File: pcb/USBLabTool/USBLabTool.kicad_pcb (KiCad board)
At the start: 4 copper layers, 79.4 x 56.2 mm, 227 parts, among them J1 Conn_01x06_Pin, J17 2x01, J19 T_N5V, J2 Conn_02x12_Odd_Even, J20 USB_C_Receptacle, K1 G5V-2, K2 G5V-2, Q1 STL11N3LLH6, SW1 TS02-66-73-BK-100-SCR-D, U1 AQY284SX, U10 MC33274ADR2G, U11 DG403, U12 STM32H562VGTx, U13 R1283K002A, U14 ST1L05APU33R, U15 ST1L05APU33R, U16 LTC1983ES6-5TRMPBF, U17 TCPP01-M12, U18 74HC245, U19 USBLC6-2SC6, U2 AQY284SX, U20 74HC245, U3 CD74HC4316, U4 LMP7718, U5 CD74HC4316, U6 LMP7718, U7 OPA863, U8 OPA863, U9 MC33274ADR2G, Y1 32.768kHz, Y2 NX2016SA-25M-EXS00A-CS08742

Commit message: fixes
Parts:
- added JP3: SJ, Jumper:SolderJumper-2_P1.3mm_Open_RoundedPad1.0x1.5mm, F.Cu at (124.1, 67.7)
- added JP4: SJ, Jumper:SolderJumper-2_P1.3mm_Open_RoundedPad1.0x1.5mm, B.Cu at (138.8, 68.1)
- added JP5: SJ, Jumper:SolderJumper-2_P1.3mm_Open_RoundedPad1.0x1.5mm, B.Cu at (113.4, 72.2)
- added JP6: SJ, Jumper:SolderJumper-2_P1.3mm_Open_RoundedPad1.0x1.5mm, F.Cu at (150.9, 99.9)
- added JP7: SJ, Jumper:SolderJumper-2_P1.3mm_Open_RoundedPad1.0x1.5mm, F.Cu at (150.9, 102.8)
- added R82: 0, Resistor_SMD:R_0603_1608Metric_Pad0.98x0.95mm_HandSolder, B.Cu at (159.3, 94.4)
- added R83: 0, Resistor_SMD:R_0603_1608Metric_Pad0.98x0.95mm_HandSolder, B.Cu at (149.8, 94.1)
- added R84: 5.1k, Resistor_SMD:R_0603_1608Metric_Pad0.98x0.95mm_HandSolder, F.Cu at (140.7, 67.3)
- added R85: 5.1k, Resistor_SMD:R_0603_1608Metric_Pad0.98x0.95mm_HandSolder, B.Cu at (116.1, 76.8)
- C59, C60: value 4.7uF -> 100nF
- C70: value 10nF -> DNF
- L5, L6: value 47uH -> 4.7uH; footprint Inductor_SMD:L_0603_1608Metric_Pad1.05x0.95mm_HandSolder -> userfp:IND_TAIYO_NRH2410_TAY
- moved D1 1.19 mm to (186.7, 103.5)
- moved L6 0.91 mm to (187.1, 107.0)
- moved L5 0.88 mm to (136.9, 78.7)
- moved C75 0.58 mm to (147.3, 92.1)
- moved C72 0.31 mm to (131.9, 70.3)
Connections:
- C33 pad 1: RCC_OSC_IN -> Net-(JP6-B)
- C34 pad 2: RCC_OSC_OUT -> Net-(JP7-A)
- C35 pad 2: RCC_OSC32_IN -> Net-(C35-Pad2)
- C36 pad 2: RCC_OSC32_OUT -> Net-(C36-Pad2)
- C70 pad 1: +5V -> Net-(D10-A)
- C72 pad 2: UCPD_CC1 -> Net-(J20-CC1)
- C73 pad 2: UCPD_CC2 -> Net-(J20-CC2)
- C74 pad 2: +5V -> Net-(D10-A)
- D10 pad 2: +5V -> Net-(D10-A)
- D3 pad 1: +3.3VA -> GNDA
- D3 pad 2: GNDA -> +3.3VA
- D4 pad 1: +3.3VA -> GNDA
- D4 pad 2: GNDA -> +3.3VA
- D9 pad C: +5V -> Net-(D10-A)
- J20 pad A4: +5V -> Net-(D10-A)
- J20 pad A5: UCPD_CC1 -> Net-(J20-CC1)
- J20 pad A9: +5V -> Net-(D10-A)
- J20 pad B4: +5V -> Net-(D10-A)
- J20 pad B5: UCPD_CC2 -> Net-(J20-CC2)
- J20 pad B9: +5V -> Net-(D10-A)
- Q1 pad 5: +5V -> Net-(D10-A)
- R67 pad 1: +5V -> Net-(D10-A)
- U12 pad 52: UCPD_CC1 -> Net-(U12-PB13)
- U12 pad 53: UCPD_CC2 -> Net-(U12-PB14)
- U17 pad 7: UCPD_CC1 -> Net-(J20-CC1)
- U17 pad 9: UCPD_CC2 -> Net-(J20-CC2)
- Y1 pad 1: RCC_OSC32_OUT -> Net-(C36-Pad2)
- Y1 pad 2: RCC_OSC32_IN -> Net-(C35-Pad2)
- Y2 pad 1: RCC_OSC_IN -> Net-(JP6-B)
- Y2 pad 3: RCC_OSC_OUT -> Net-(JP7-A)
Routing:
- net Net-(D10-A): track 0.00 -> 84.6 mm, vias 0 -> 7
- net +5V: track 252.2 -> 211.6 mm, vias 11 -> 9
- net Net-(J20-CC1): track 0.00 -> 29.2 mm, vias 0 -> 3
- net Net-(J20-CC2): track 0.00 -> 27.9 mm, vias 0 -> 2
- net Net-(U12-PB13): track 0.00 -> 26.9 mm, vias 0 -> 3
- net Net-(U12-PB14): track 0.00 -> 26.4 mm, vias 0 -> 2
- net Net-(JP7-A): track 0.00 -> 18.4 mm, vias 0 -> 2
- net UCPD_CC1: track 37.8 -> 20.8 mm, vias 4 -> 1
- net RCC_OSC_OUT: track 8.50 -> 24.6 mm, vias 0 -> 2
- net Net-(JP6-B): track 0.00 -> 10.9 mm
- net UCPD_CC2: track 55.7 -> 48.7 mm, vias 5 -> 4
- net RCC_OSC_IN: track 4.02 -> 10.7 mm
- net Net-(C36-Pad2): track 0.00 -> 5.34 mm
- net Net-(C35-Pad2): track 0.00 -> 4.14 mm
- net +3.3V: track 141.5 -> 144.9 mm, vias 11 -> 13
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
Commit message: Update USBLabTool.kicad_pcb
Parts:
- moved JP7 1.20 mm to (151.8, 103.5)
- moved JP6 1.03 mm to (151.0, 101.0)
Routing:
- net RCC_OSC_IN: track 10.7 -> 11.7 mm
- net Net-(JP6-B): track 10.9 -> 11.9 mm
- net Net-(JP7-A): track 18.4 -> 17.7 mm
- net RCC_OSC_OUT: track 24.6 -> 24.0 mm
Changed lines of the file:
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@@
 		(tags "LQFP QFP")
 		(property "Reference" "U12"
-			(at -8.025 -7.95 0)
+			(at -7.794 -7.856 0)
 			(layer "F.SilkS")
 			(effects
@@
 	(footprint "Jumper:SolderJumper-2_P1.3mm_Open_RoundedPad1.0x1.5mm"
 		(layer "F.Cu")
-		(at 150.9 102.8 180)
+		(at 151.85 103.525 180)
 		(descr "SMD Solder Jumper, 1x1.5mm, rounded Pads, 0.3mm gap, open")
 		(tags "solder jumper open")
 		(property "Reference" "JP7"
-			(at 0 -1.8 0)
+			(at -3.1 0.025 0)
 			(layer "F.SilkS")
 			(effects
@@
 	(footprint "Jumper:SolderJumper-2_P1.3mm_Open_RoundedPad1.0x1.5mm"
 		(layer "F.Cu")
-		(at 150.95 99.925)
+		(at 151 100.95)
 		(descr "SMD Solder Jumper, 1x1.5mm, rounded Pads, 0.3mm gap, open")
 		(tags "solder jumper open")
 		(property "Reference" "JP6"
-			(at 0 -1.8 0)
+			(at -2.125 2 0)
 			(layer "F.SilkS")
 			(effects
@@
 	)
 	(gr_text "RESET"
-		(at 155.106 105.244 0)
+		(at 155.775 103.675 0)
 		(layer "F.SilkS")
 		(effects
@@
 	)
 	(segment
-		(start 150.3 99.1)
-		(end 150.3 99.925)
+		(start 152.625 92.625)
+		(end 152.625 97.85)
 		(width 0.2)
 		(layer "F.Cu")
@@
 	)
 	(segment
-		(start 152.625 96.775)
-		(end 150.3 99.1)
+		(start 150.35 100.125)
+		(end 150.35 100.95)
 		(width 0.2)
 		(layer "F.Cu")
@@
 	)
 	(segment
-		(start 152.625 92.625)
-		(end 152.625 96.775)
+		(start 152.625 97.85)
+		(end 150.35 100.125)
 		(width 0.2)
 		(layer "F.Cu")
@@
 	)
 	(segment
-		(start 156.5 97.45)
-		(end 156.5 100.075)
+		(start 149.331 91.294)
+		(end 148.375 92.25)
 		(width 0.2)
 		(layer "F.Cu")
@@
 	)
 	(segment
-		(start 149.331 91.294)
-		(end 148.375 92.25)
+		(start 156.5 97.45)
+		(end 156.525 97.425)
 		(width 0.2)
 		(layer "F.Cu")
@@
 	)
 	(segment
-		(start 151 101.5)
-		(end 150.25 102.25)
+		(start 151.2 103.525)
+		(end 151.2 102.95)
 		(width 0.2)
 		(layer "F.Cu")
@@
 	)
 	(segment
-		(start 156.525 97.425)
-		(end 156.5 97.45)
+		(start 151.875 102.275)
+		(end 154.3 102.275)
 		(width 0.2)
 		(layer "F.Cu")
@@
 	)
 	(segment
-		(start 150.25 102.25)
-		(end 150.25 102.8)
+		(start 151.2 102.95)
+		(end 151.875 102.275)
 		(width 0.2)
 		(layer "F.Cu")
@@
 	(segment
 		(start 156.5 100.075)
-		(end 155.075 101.5)
+		(end 156.5 97.45)
 		(width 0.2)
 		(layer "F.Cu")
@@
 	)
 	(segment
-		(start 155.375 96.275)
-		(end 156.525 97.425)
+		(start 154.3 102.275)
+		(end 156.5 100.075)
 		(width 0.2)
 		(layer "F.Cu")
@@
 	)
 	(segment
-		(start 155.075 101.5)
-		(end 151 101.5)
+		(start 156.525 97.425)
+		(end 155.375 96.275)
 		(width 0.2)
 		(layer "F.Cu")
@@
 	)
 	(segment
+		(start 129.215 70.79)
+		(end 129.215 72.915)
+		(width 0.2)
+		(layer "F.Cu")
+		(net 189)
+	)
+	(segment
 		(start 129.325 73.025)
 		(end 129.275 73.025)
@@
 	)
 	(segment
-		(start 129.275 73.025)
-		(end 126.556 75.744)
+		(start 129.215 72.915)
+		(end 129.325 73.025)
 		(width 0.2)
 		(layer "F.Cu")
@@
 	)
 	(segment
-		(start 129.215 70.79)
-		(end 129.215 72.735)
+		(start 129.275 73.025)
+		(end 126.556 75.744)
 		(width 0.2)
 		(layer "F.Cu")
@@
 	)
 	(segment
-		(start 153.435 91.91)
-		(end 153.435 93.25)
+		(start 151.925 99.6)
+		(end 154.775 96.75)
 		(width 0.2)
 		(layer "F.Cu")
@@
 	)
 	(segment
-		(start 151.6 99.925)
-		(end 154.775 96.75)
+		(start 153.435 91.91)
+		(end 153.435 93.25)
 		(width 0.2)
 		(layer "F.Cu")
@@
 	)
 	(segment
+		(start 151.65 100.95)
+		(end 151.65 99.875)
+		(width 0.2)
+		(layer "F.Cu")
+		(net 213)
+	)
+	(segment
 		(start 153.075 91.55)
 		(end 153.435 91.91)
@@
 	)
 	(segment
+		(start 151.65 99.875)
+		(end 151.925 99.6)
+		(width 0.2)
+		(layer "F.Cu")
+		(net 213)
+	)
+	(segment
 		(start 152.75 91.55)
 		(end 153.075 91.55)
@@
 	)
 	(segment
-		(start 153.375 102.8)
-		(end 151.55 102.8)
+		(start 154.35 102.75)
+		(end 153.425 102.75)
 		(width 0.2)
 		(layer "F.Cu")
@@
 	)
 	(segment
-		(start 156.975 100.125)
-		(end 154.35 102.75)
+		(start 152.65 103.525)
+		(end 152.5 103.525)
 		(width 0.2)
 		(layer "F.Cu")
@@
 	)
 	(segment
-		(start 154.35 102.75)
-		(end 153.425 102.75)
+		(start 154.975 90.5)
+		(end 155.25 90.775)
 		(width 0.2)
 		(layer "F.Cu")
@@
 	)
 	(segment
-		(start 156.95 96.85)
-		(end 156.975 96.875)
+		(start 156.975 100.125)
+		(end 154.35 102.75)
 		(width 0.2)
 		(layer "F.Cu")
@@
 	)
 	(segment
-		(start 156.975 96.875)
-		(end 156.975 100.125)
+		(start 154.1 90.5)
+		(end 154.975 90.5)
 		(width 0.2)
 		(layer "F.Cu")
@@
 	)
 	(segment
-		(start 154.975 90.5)
-		(end 155.25 90.775)
+		(start 156.975 96.875)
+		(end 156.975 100.125)
 		(width 0.2)
 		(layer "F.Cu")
@@
 	)
 	(segment
-		(start 154.1 90.5)
-		(end 154.975 90.5)
+		(start 153.425 102.75)
+		(end 152.65 103.525)
 		(width 0.2)
 		(layer "F.Cu")
@@
 	)
 	(segment
-		(start 153.425 102.75)
-		(end 153.375 102.8)
+		(start 156.95 96.85)
+		(end 156.875 96.925)
 		(width 0.2)
 		(layer "F.Cu")
@@
 	)
 	(segment
-		(start 156.95 96.85)
-		(end 156.875 96.925)
+		(start 155.7 91.225)
+		(end 155.7 93.25)
 		(width 0.2)
 		(layer "F.Cu")
@@
 	)
 	(segment
-		(start 155.7 91.225)
-		(end 155.7 93.25)
+		(start 156.95 96.85)
+		(end 156.975 96.875)
 		(width 0.2)
 		(layer "F.Cu")

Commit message: V2 fixed
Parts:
- added JP8: SJ, Jumper:SolderJumper-2_P1.3mm_Open_RoundedPad1.0x1.5mm, F.Cu at (160.7, 102.8)
- added JP9: SJ, Jumper:SolderJumper-2_P1.3mm_Open_RoundedPad1.0x1.5mm, F.Cu at (157.2, 102.8)
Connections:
- R82 pad 1: RCC_OSC32_IN -> Net-(JP8-B)
- R83 pad 1: RCC_OSC32_OUT -> Net-(JP9-B)
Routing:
- net Net-(JP9-B): track 0.00 -> 13.8 mm, vias 0 -> 2
- net Net-(JP8-B): track 0.00 -> 9.17 mm, vias 0 -> 1
- net RCC_OSC32_OUT: track 4.81 -> 13.1 mm, vias 1 -> 2
- net RCC_OSC32_IN: track 11.0 -> 16.5 mm, vias 1 -> 2
- net Net-(U15-VO): track 9.24 -> 12.2 mm
- net RCC_OSC_OUT: track 24.0 -> 23.0 mm
- net Net-(JP7-A): track 17.7 -> 16.9 mm

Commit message: PCB V2 updates
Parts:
- removed CR2: ESDALC6V1-1U2, userfp:DIODE_ESDALC6V1-1U2_STM
- removed JP8, JP9: SJ, Jumper:SolderJumper-2_P1.3mm_Open_RoundedPad1.0x1.5mm
- added CR1: ESDALC6V1-1M2, Diode_SMD:D_SOD-882, B.Cu at (148.8, 91.3)
- added H3: MountingHole, MountingHole:MountingHole_2.2mm_M2, F.Cu at (113.0, 79.2)
- added H4: MountingHole, MountingHole:MountingHole_2.2mm_M2, F.Cu at (186.2, 118.8)
- added TP15: TestPoint, TestPoint:TestPoint_Pad_2.0x2.0mm, B.Cu at (147.2, 79.8)
- added TP16: TestPoint, TestPoint:TestPoint_Pad_2.0x2.0mm, B.Cu at (129.3, 98.5)
- added TP17: TestPoint, TestPoint:TestPoint_Pad_2.0x2.0mm, B.Cu at (114.8, 102.0)
- added TP18: TestPoint, TestPoint:TestPoint_Pad_2.0x2.0mm, F.Cu at (154.6, 67.8)
- added TP19: TestPoint, TestPoint:TestPoint_Pad_2.0x2.0mm, F.Cu at (137.2, 75.4)
- added TP20: TestPoint, TestPoint:TestPoint_Pad_2.0x2.0mm, B.Cu at (143.8, 70.0)
- added TP21: TestPoint, TestPoint:TestPoint_Pad_2.0x2.0mm, B.Cu at (143.3, 79.8)
- added TP22: TestPoint, TestPoint:TestPoint_Pad_2.0x2.0mm, B.Cu at (183.4, 73.7)
- added TP23: TestPoint, TestPoint:TestPoint_Pad_2.0x2.0mm, B.Cu at (169.6, 73.0)
- added TP24: TestPoint, TestPoint:TestPoint_Pad_2.0x2.0mm, B.Cu at (142.8, 99.9)
- added TP25: TestPoint, TestPoint:TestPoint_Pad_2.0x2.0mm, B.Cu at (139.8, 101.8)
- C18, C59, C66, JP3, R10: moved to B.Cu
- TP7: footprint TestPoint:TestPoint_Pad_D2.0mm -> TestPoint:TestPoint_Pad_2.0x2.0mm
- U12: value STM32H562VGTx -> STM32H563VITx
- moved C57 23.1 mm to (166.7, 77.5)
- moved C54 21.1 mm to (164.7, 75.5)
- moved R85 17.1 mm to (132.8, 72.9)
- moved J17 16.6 mm to (111.8, 97.9)
- moved JP3 15.1 mm to (139.1, 69.7), turned to 90 degrees
- moved C63 8.00 mm to (185.3, 112.3), turned to 90 degrees
- moved C64 7.57 mm to (186.9, 112.3), turned to 90 degrees
- moved JP5 7.20 mm to (118.3, 77.4), turned to 180 degrees
- moved TP4 5.81 mm to (127.9, 77.0)
- moved C66 5.48 mm to (183.8, 112.4), turned to 90 degrees
- moved C59 4.96 mm to (133.2, 79.3), turned to 90 degrees
- moved C75 3.42 mm to (150.7, 91.5)
- moved R10 3.15 mm to (166.0, 72.0), turned to 0 degrees
- moved R67 3.11 mm to (125.0, 70.4), turned to -90 degrees
- moved JP7 2.73 mm to (154.4, 102.7)
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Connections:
- R82 pad 1: Net-(JP8-B) -> RCC_OSC32_IN
- R83 pad 1: Net-(JP9-B) -> RCC_OSC32_OUT
- U12 pad 1: unconnected-(U12-PE2-Pad1) -> CH1_attenuate
- U12 pad 15: unconnected-(U12-PC0-Pad15) -> CH1_amp_5
- U12 pad 16: unconnected-(U12-PC1-Pad16) -> CH1_amp_2.5
- U12 pad 26: GAIN_C0 -> unconnected-(U12-PA3-Pad26)
- U12 pad 32: GAIN_C1 -> unconnected-(U12-PA7-Pad32)
- U12 pad 34: CH1_attenuate -> CH1_amp_1
- U12 pad 35: CH1_amp_1 -> CH1_amp_10
- U12 pad 36: CH1_amp_5 -> CH0_amp_1
- U12 pad 37: CH1_amp_2.5 -> CH0_amp_10
- U12 pad 43: unconnected-(U12-PE12-Pad43) -> CH0_amp_5
- U12 pad 44: unconnected-(U12-PE13-Pad44) -> CH0_amp_2.5
- U12 pad 47: CH1_amp_10 -> unconnected-(U12-PB10-Pad47)
- U12 pad 51: CH0_amp_1 -> unconnected-(U12-PB12-Pad51)
- U12 pad 54: CH0_amp_10 -> unconnected-(U12-PB15-Pad54)
- U12 pad 63: CH0_amp_2.5 -> GAIN_C1
- U12 pad 64: unconnected-(U12-PC7-Pad64) -> GAIN_C0
- U12 pad 65: CH0_amp_5 -> unconnected-(U12-PC8-Pad65)
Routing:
- net UCPD_CC2: track 48.7 -> 22.5 mm
- net GNDA: track 332.5 -> 311.9 mm, vias 26 -> 28
- net CH1_attenuate: track 61.6 -> 41.8 mm, vias 3 -> 1
- net CH1_amp_2.5: track 35.0 -> 16.3 mm, vias 3 -> 2
- net +5V: track 211.6 -> 197.2 mm, vias 9 -> 8
- net Net-(JP9-B): track 13.8 -> 0.00 mm, vias 2 -> 0
- net GND: track 270.6 -> 258.6 mm, vias 32 -> 30
- net GAIN_C1: track 25.8 -> 15.6 mm
- net GAIN_C0: track 30.7 -> 21.0 mm
- net Net-(U12-PB14): track 26.4 -> 16.7 mm
- net Net-(JP8-B): track 9.17 -> 0.00 mm, vias 1 -> 0
- net CH1_amp_5: track 24.7 -> 15.6 mm, vias 3 -> 2
- net RCC_OSC32_OUT: track 13.1 -> 4.81 mm, vias 2 -> 1
- net UCPD_FLT: track 43.8 -> 36.3 mm, vias 4 -> 5
- net CH0_amp_2.5: track 20.3 -> 13.0 mm
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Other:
- board text added: "ECE USB Multi-Function Lab Instrument II"
- board text removed: "ECE USB Multi-Function Lab Instrument"

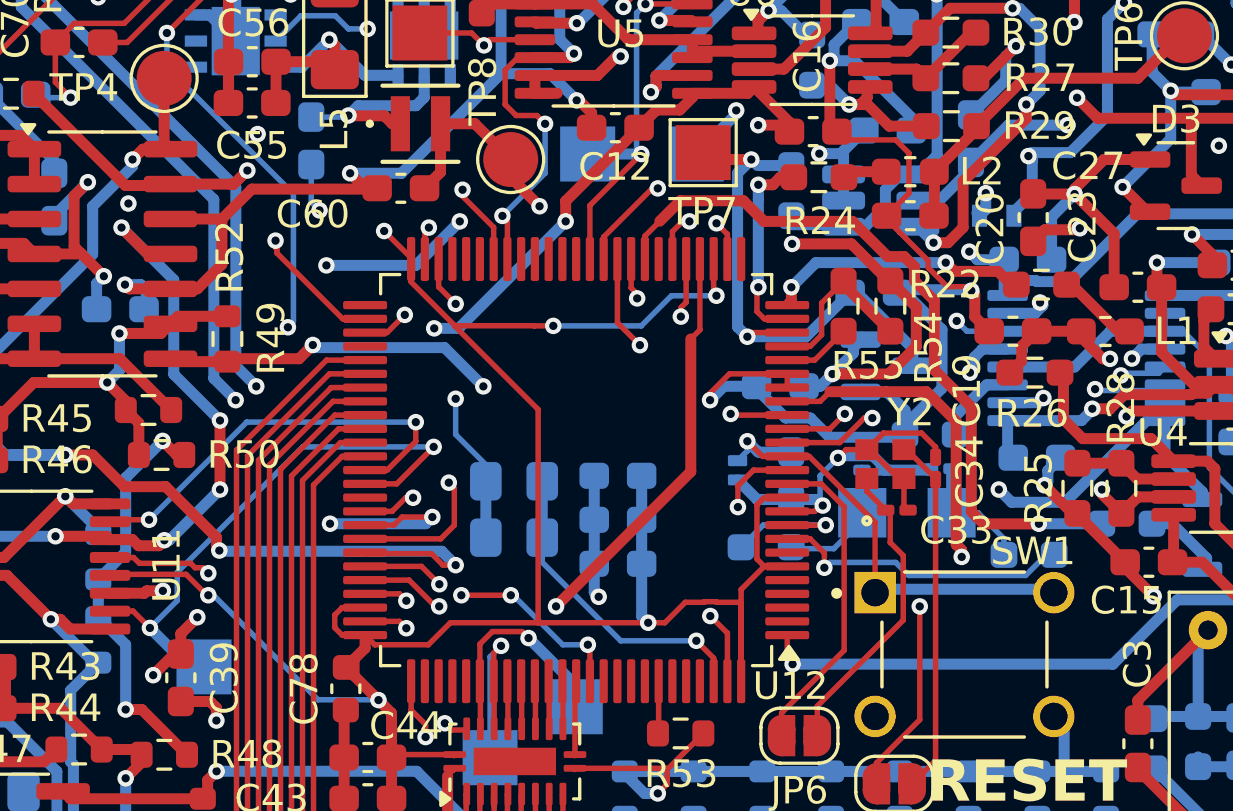
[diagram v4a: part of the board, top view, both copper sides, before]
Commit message: add pads for 32kHz crystal
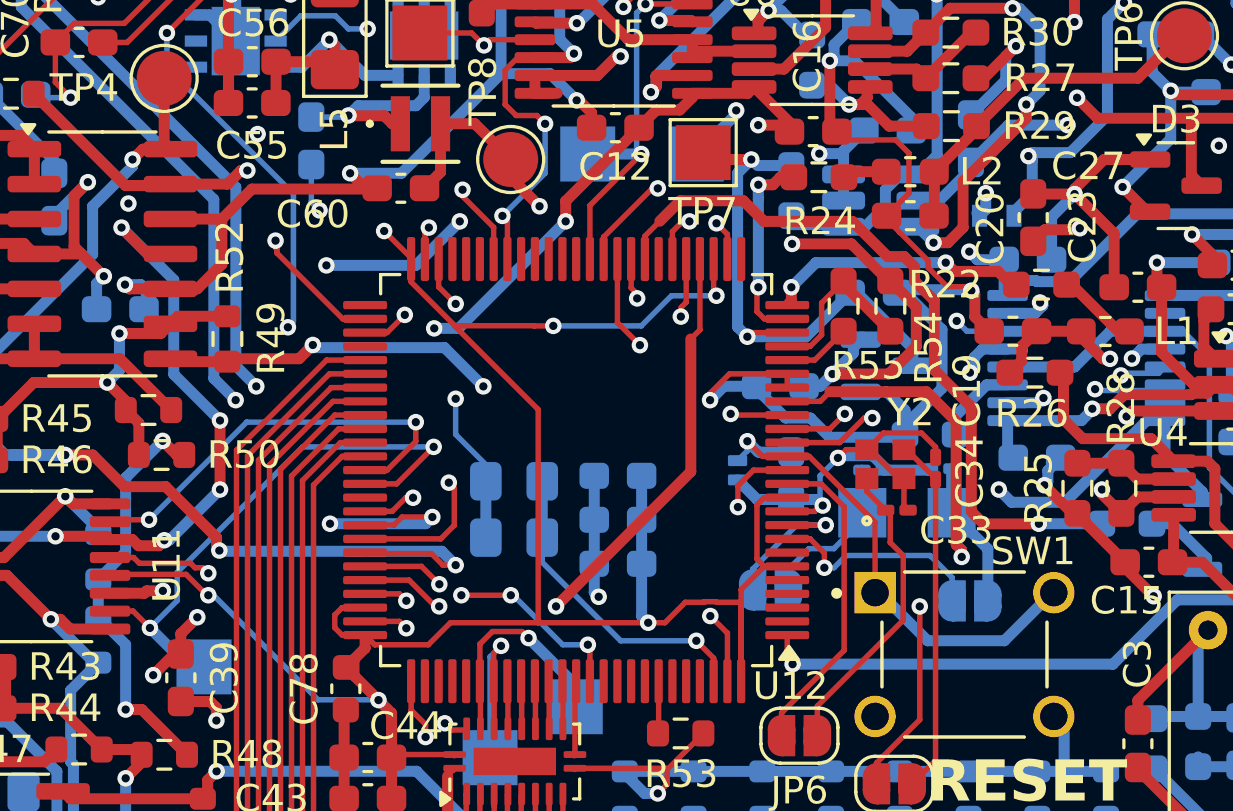
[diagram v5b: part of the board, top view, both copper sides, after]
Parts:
- removed R82, R83: 0, Resistor_SMD:R_0603_1608Metric_Pad0.98x0.95mm_HandSolder
- added JP8: SJ, Jumper:SolderJumper-2_P1.3mm_Open_RoundedPad1.0x1.5mm, B.Cu at (157.2, 96.0)
- added JP9: SJ, Jumper:SolderJumper-2_P1.3mm_Open_RoundedPad1.0x1.5mm, B.Cu at (149.9, 95.7)
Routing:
- net RCC_OSC32_IN: track 11.0 -> 8.11 mm
- net NRST: track 86.2 -> 87.7 mm
- net Net-(JP9-B): track 5.50 -> 6.64 mm
- net Net-(JP8-B): track 4.49 -> 5.36 mm
- net RCC_OSC32_OUT: track 4.81 -> 5.47 mm
